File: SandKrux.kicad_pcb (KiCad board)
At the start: 2 copper layers, 58.3 x 98.2 mm, 177 parts, among them CN2 SM02B-PASS-TBT(LF)(SN), CN3 1.25mm-2P socket, IC1 TROPIC01_chip, Q1 S8050, SW1 TL3330AF130QG, SW2 TL3330AF130QG, SW3 TL3330AF130QG, SW4 TL3330AF130QG, SW5 TL3330AF130QG, U1 K210_C913414, U10 AXP173_C3345106, U12 PCIE-67P42H, U13 CH552T, U2 MT9700, U3 XC6206-3.3V, U4 XC6206P182MR_C347373, U5 GD25LQ128EWIGR, U6 TMI7003C, U7 SGM803-TXN3/TR_C5152602, U8 XC6206P302MR_C347375, U9 HX TF-CARD XG8P H1.5, X1 X322526MMB4SI

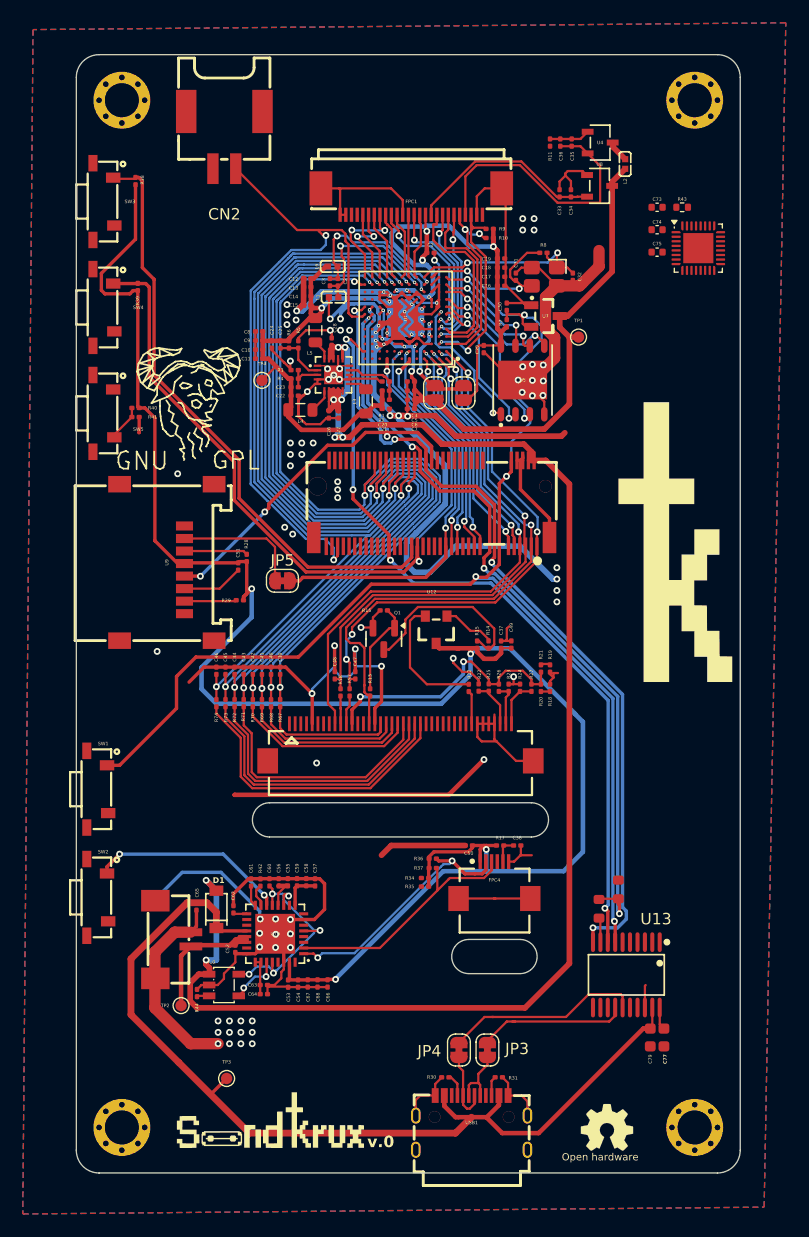
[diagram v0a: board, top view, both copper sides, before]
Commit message: troca de resistores por pecas jlcpcb
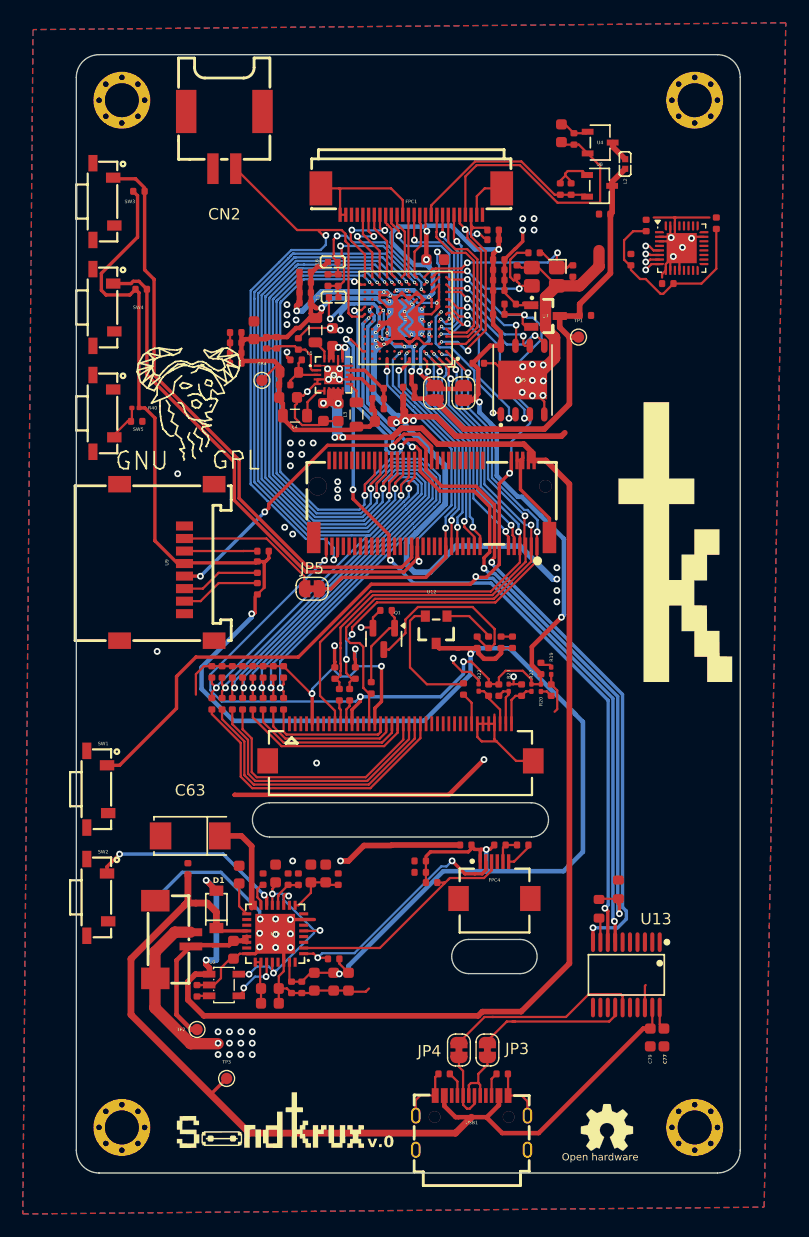
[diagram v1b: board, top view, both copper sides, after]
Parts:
- removed C61: 220uF, Capacitor_SMD:C_0201_0603Metric
- removed C64, C67, C68: 22uF, Capacitor_SMD:C_0201_0603Metric
- removed C65: 10uF, Capacitor_SMD:C_0201_0603Metric
- removed C73, C74, C75: 100n, Capacitor_SMD:C_0402_1005Metric
- removed R41: 0R, Resistor_SMD:R_0201_0603Metric
- removed R43: 47k, Resistor_SMD:R_0402_1005Metric
- removed R44: 10K, Resistor_SMD:R_0201_0603Metric
- removed R67, R68, R69, R70, R71, R72, R73, R74: 100R, Resistor_SMD:R_0201_0603Metric
- added C69: 1uF, PCM_JLCPCB:C_0603, F.Cu at (94.5, 160.7)
- added C70: 1uF, PCM_JLCPCB:C_0603, F.Cu at (97.7, 160.6)
- added C71: 100nF, PCM_JLCPCB:C_0402, F.Cu at (109.4, 118.8)
- added C72: 100nF, PCM_JLCPCB:C_0402, F.Cu at (109.4, 117.9)
- added C76: 10uF, PCM_JLCPCB:C_0402, F.Cu at (94.2, 115.8)
- added C78: 10uF, PCM_JLCPCB:C_0402, F.Cu at (94.2, 114.9)
- added C80: 10uF, PCM_JLCPCB:C_0402, F.Cu at (94.2, 114.0)
- added C81: 10uF, PCM_JLCPCB:C_0402, F.Cu at (94.2, 113.1)
- added R45: 150kΩ, PCM_JLCPCB:R_0402, F.Cu at (106.7, 118.9)
- added R46: 2kΩ, PCM_JLCPCB:R_0402, F.Cu at (116.8, 105.0)
- added R47: 100Ω, PCM_JLCPCB:R_0402, F.Cu at (116.4, 140.3)
- added R48: 5.1kΩ, PCM_JLCPCB:R_0402, F.Cu at (119.3, 144.5)
- added R54: 100Ω, PCM_JLCPCB:R_0402, F.Cu at (94.8, 145.7)
- added R55: 100Ω, PCM_JLCPCB:R_0402, F.Cu at (95.7, 145.7)
- added R56: 100Ω, PCM_JLCPCB:R_0402, F.Cu at (96.6, 145.7)
- added R59: 100Ω, PCM_JLCPCB:R_0402, F.Cu at (92.1, 145.7)
- added R60: 100Ω, PCM_JLCPCB:R_0402, F.Cu at (98.4, 145.7)
- added R61: 100Ω, PCM_JLCPCB:R_0402, F.Cu at (97.5, 145.7)
- C1, C52, C57: footprint Capacitor_SMD:C_0201_0603Metric -> PCM_JLCPCB:C_0603
- C10, C11: value 10uF -> 100nF; footprint Capacitor_SMD:C_0201_0603Metric -> PCM_JLCPCB:C_0402
- C12, C13, C14, C55, C58: value 10uF -> 22uF; footprint Capacitor_SMD:C_0201_0603Metric -> PCM_JLCPCB:C_0603
- C15, C16, C17: value 10uF -> 18pF; footprint Capacitor_SMD:C_0201_0603Metric -> PCM_JLCPCB:C_0402
- C18, C19, C49, C56: value 100nF -> 22uF; footprint Capacitor_SMD:C_0201_0603Metric -> PCM_JLCPCB:C_0603
- C2, C37, C39, C40, C50, C53, C8, C9: footprint Capacitor_SMD:C_0201_0603Metric -> PCM_JLCPCB:C_0402
- C20, C25: value 18pF -> 22uF; footprint Capacitor_SMD:C_0201_0603Metric -> PCM_JLCPCB:C_0603
- C21, C26, C27, C59, C66: value 22uF -> 10uF; footprint Capacitor_SMD:C_0201_0603Metric -> PCM_JLCPCB:C_0402
- C22, C24, C28: value 22uF -> 100nF; footprint Capacitor_SMD:C_0201_0603Metric -> PCM_JLCPCB:C_0402
- C23: value 18pF -> 6pF; footprint Capacitor_SMD:C_0201_0603Metric -> PCM_JLCPCB:C_0402
- C29, C30, C34, C38: value 100nF -> 100pF; footprint Capacitor_SMD:C_0201_0603Metric -> PCM_JLCPCB:C_0402
- C3: value 10uF -> 6pF; footprint Capacitor_SMD:C_0201_0603Metric -> PCM_JLCPCB:C_0402
- C31, C32: value 6pF -> 100pF; footprint Capacitor_SMD:C_0201_0603Metric -> PCM_JLCPCB:C_0402
- C33, C36: value 10uF -> 100pF; footprint Capacitor_SMD:C_0201_0603Metric -> PCM_JLCPCB:C_0402
- C35: value 22uF -> 100pF; footprint Capacitor_SMD:C_0201_0603Metric -> PCM_JLCPCB:C_0402
- C4, C5, C6, C7: value 100nF -> 10uF; footprint Capacitor_SMD:C_0201_0603Metric -> PCM_JLCPCB:C_0402
- C41, C43: value 100pF -> 10uF; footprint Capacitor_SMD:C_0201_0603Metric -> PCM_JLCPCB:C_0402
- C42, C44, C45, C46: value 100pF -> 100nF; footprint Capacitor_SMD:C_0201_0603Metric -> PCM_JLCPCB:C_0402
- C47, C48: value 100pF -> 22uF; footprint Capacitor_SMD:C_0201_0603Metric -> PCM_JLCPCB:C_0603
- C51: value 10uF -> 1nF; footprint Capacitor_SMD:C_0201_0603Metric -> PCM_JLCPCB:C_0402
- C54: value 1nF -> 100nF; footprint Capacitor_SMD:C_0201_0603Metric -> PCM_JLCPCB:C_0402
- C60, C62: value 1uF -> 100nF; footprint Capacitor_SMD:C_0201_0603Metric -> PCM_JLCPCB:C_0402
- C63: value 220nF -> TAJC227K006RNJ; footprint Capacitor_SMD:C_0201_0603Metric -> easyeda2kicad:CAP-SMD_L6.0-W3.2-R-RD
- R1: value 300k 1% -> 680kΩ; footprint Resistor_SMD:R_0201_0603Metric -> PCM_JLCPCB:R_0603
- R10: value 2K -> 100Ω; footprint Resistor_SMD:R_0201_0603Metric -> PCM_JLCPCB:R_0402
- R11: value 0R -> 100Ω; footprint Resistor_SMD:R_0201_0603Metric -> PCM_JLCPCB:R_0402
- R12: value 5.1R -> 100Ω; footprint Resistor_SMD:R_0201_0603Metric -> PCM_JLCPCB:R_0402
- R13: value 100R -> 10kΩ; footprint Resistor_SMD:R_0201_0603Metric -> PCM_JLCPCB:R_0402
- R14: value 100R -> 0Ω; footprint Resistor_SMD:R_0201_0603Metric -> PCM_JLCPCB:R_0402
- R15, R17, R28: value 10K -> 10kΩ; footprint Resistor_SMD:R_0201_0603Metric -> PCM_JLCPCB:R_0402
- R16: value 10K -> 0Ω; footprint Resistor_SMD:R_0201_0603Metric -> PCM_JLCPCB:R_0402
- R18, R21: value 0R -> 5.1kΩ; footprint Resistor_SMD:R_0201_0603Metric -> PCM_JLCPCB:R_0402
- R2, R3: value 150k 1% -> 150kΩ; footprint Resistor_SMD:R_0201_0603Metric -> PCM_JLCPCB:R_0402
- R24, R25, R26: value 5.1K -> 1.5kΩ; footprint Resistor_SMD:R_0201_0603Metric -> PCM_JLCPCB:R_0402
- R29: value 10K -> 47kΩ; footprint Resistor_SMD:R_0201_0603Metric -> PCM_JLCPCB:R_0402
- R30, R31: value 5.1K -> 5.1kΩ; footprint Resistor_SMD:R_0201_0603Metric -> PCM_JLCPCB:R_0402
- R34, R35, R36: value 1.5K -> 1.5kΩ; footprint Resistor_SMD:R_0201_0603Metric -> PCM_JLCPCB:R_0402
- R37, R38: value 1.5K -> 10kΩ; footprint Resistor_SMD:R_0201_0603Metric -> PCM_JLCPCB:R_0402
- R39: value 1.5K -> 200kΩ; footprint Resistor_SMD:R_0201_0603Metric -> PCM_JLCPCB:R_0402
- R4: value 680k 1% -> 12kΩ; footprint Resistor_SMD:R_0201_0603Metric -> PCM_JLCPCB:R_0402
- R42: value 200K -> 0Ω; footprint Resistor_SMD:R_0201_0603Metric -> PCM_JLCPCB:R_0402
- R5: value 150k 1% -> 300kΩ; footprint Resistor_SMD:R_0201_0603Metric -> PCM_JLCPCB:R_0402
- R57, R58: value 100R -> 100Ω; footprint Resistor_SMD:R_0201_0603Metric -> PCM_JLCPCB:R_0402
- R6: value 300k 1% -> 300kΩ; footprint Resistor_SMD:R_0201_0603Metric -> PCM_JLCPCB:R_0402
- R7: value 12K -> 1MΩ; footprint Resistor_SMD:R_0201_0603Metric -> PCM_JLCPCB:R_0402
- R8: value 1M -> 2kΩ; footprint Resistor_SMD:R_0201_0603Metric -> PCM_JLCPCB:R_0402
- R9: value 2K -> 5.1kΩ; footprint Resistor_SMD:R_0201_0603Metric -> PCM_JLCPCB:R_0402
- moved R38 71.3 mm to (90.8, 170.9), turned to -90 degrees
- moved C60 65.6 mm to (126.6, 102.7), turned to 180 degrees
- moved C62 60.6 mm to (124.9, 111.6), turned to 0 degrees
- moved C44 57.7 mm to (136.4, 103.5)
- moved C35 55.7 mm to (93.0, 142.9)
- moved C36 55.6 mm to (92.1, 142.9)
- moved C46 54.3 mm to (130.2, 103.7)
- moved R25 53.3 mm to (85.7, 100.7), turned to 0 degrees
- moved R39 53.2 mm to (96.6, 161.1), turned to -90 degrees
- moved C45 51.6 mm to (132.1, 108.8), turned to 180 degrees
- moved R11 51.6 mm to (104.2, 144.9), turned to 90 degrees
- moved C34 51.5 mm to (93.9, 142.9)
- moved C33 50.4 mm to (94.8, 142.9)
- moved R24 48.3 mm to (85.9, 109.3), turned to 0 degrees
- moved R29 45.5 mm to (128.9, 106.7), turned to 90 degrees
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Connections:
- C1 pad 1: /k210/1V8 -> /VCC_1V83V3
- C10 pad 1: GND -> /VCC_1V83V3
- C10 pad 2: /k210/0V9 -> GND
- C11 pad 1: GND -> /VCC_1V83V3
- C11 pad 2: /k210/0V9 -> GND
- C12 pad 1: GND -> /k210/0V9
- C12 pad 2: /k210/0V9 -> GND
- C13 pad 1: GND -> /k210/0V9
- C13 pad 2: /k210/0V9 -> GND
- C14 pad 1: GND -> /k210/0V9
- C14 pad 2: /k210/0V9 -> GND
- C15 pad 1: GND -> /k210/0V9
- C15 pad 2: /k210/0V9 -> /k210/Vadj
- C16 pad 1: GND -> /k210/0V9
- C16 pad 2: /k210/1V8 -> Net-(U6-FB2)
- C17 pad 1: GND -> /k210/0V9
- C17 pad 2: /k210/1V8 -> Net-(U6-FB3)
- C18 pad 1: GND -> /5V
- C18 pad 2: /k210/1V8 -> GND
- C19 pad 1: GND -> /5V
- C19 pad 2: /k210/1V8 -> GND
- C2 pad 1: Net-(U1-VSSPLL) -> GND
- C2 pad 2: Net-(U1-VDDPLL) -> /CH552_P1.0
- C20 pad 1: /k210/Vadj -> /5V
- C20 pad 2: /k210/0V9 -> GND
- C21 pad 1: GND -> Net-(U1-VDDPLL)
- C21 pad 2: /k210/0V9 -> Net-(U1-VSSPLL)
- C22 pad 1: GND -> Net-(U1-VDDPLL)
- C22 pad 2: /k210/0V9 -> Net-(U1-VSSPLL)
- C23 pad 1: Net-(U6-FB2) -> /k210/XIN
- C23 pad 2: /k210/0V9 -> GND
- C24 pad 1: GND -> /VCC_1V83V3
- C24 pad 2: /k210/0V9 -> GND
- C25 pad 1: Net-(U6-FB3) -> /k210/CMOS-AVDD
- C25 pad 2: /k210/0V9 -> GND
- C26 pad 1: GND -> /k210/CMOS-AVDD
- C26 pad 2: /5V -> GND
- C27 pad 1: GND -> /k210/CMOS-DVDD
- C27 pad 2: /5V -> GND
- C28 pad 1: GND -> /k210/CMOS-DVDD
- C28 pad 2: /5V -> GND
- C29 pad 1: /k210/1V8 -> GND
- C29 pad 2: GND -> /LCD_D0
- C3 pad 1: Net-(U1-VSSPLL) -> GND
- C3 pad 2: Net-(U1-VDDPLL) -> /k210/XOUT
- C30 pad 2: /CH552_P1.0 -> /LCD_D1
- C31 pad 1: /k210/XOUT -> GND
- C31 pad 2: GND -> /LCD_D2
- C32 pad 2: /k210/XIN -> /LCD_D3
- C33 pad 2: /k210/CMOS-DVDD -> /LCD_D4
- C34 pad 2: /k210/CMOS-DVDD -> /LCD_D5
- C35 pad 2: /k210/CMOS-AVDD -> /LCD_D6
- C36 pad 2: /k210/CMOS-AVDD -> /LCD_D7
- C38 pad 1: /CAPTOUCH_RST -> GND
- C38 pad 2: GND -> /CAPTOUCH_RST
- C39 pad 1: /LCD_D0 -> GND
- C39 pad 2: GND -> /LCD_WR
- C4 pad 1: GND -> /k210/0V9
- C4 pad 2: +3.3V -> GND
- C40 pad 1: /LCD_D1 -> GND
- C40 pad 2: GND -> /LCD_DC
- C41 pad 1: /LCD_D2 -> GND
- C41 pad 2: GND -> /3V3
- C42 pad 1: /LCD_D3 -> /3V3
- C43 pad 1: /LCD_D4 -> /3V3
- C44 pad 1: /LCD_D5 -> VCC
- C45 pad 1: /LCD_D6 -> VCC
- C46 pad 1: /LCD_D7 -> VCC
- C47 pad 1: /LCD_WR -> /3V3
- C48 pad 1: /LCD_DC -> /3V3
- C5 pad 1: GND -> /k210/0V9
- C5 pad 2: +3.3V -> GND
- C51 pad 1: GND -> /3V3
- C51 pad 2: /3V3 -> GND
- C52 pad 1: GND -> Net-(C52-Pad1)
- C52 pad 2: /VBAT -> GND
- C53 pad 1: GND -> /VDD
- C53 pad 2: /3V3 -> GND
- C54 pad 2: /3V3 -> /VDD
- C55 pad 1: /VDD -> /ADD_3V0
- C56 pad 1: /VDD -> /ADD_3V0
- C57 pad 1: GND -> /VBAT
- C57 pad 2: /ADD_3V0 -> GND
- C58 pad 1: GND -> Net-(C52-Pad1)
- C58 pad 2: /ADD_3V0 -> GND
- C59 pad 2: /ADD_3V0 -> /5V_USB
- C6 pad 1: GND -> /k210/0V9
- C6 pad 2: +3.3V -> GND
- C60 pad 1: /IPSOUT -> +3.3V
- C62 pad 1: Net-(U10-VINT) -> +3.3V
- C63 pad 1: Net-(C63-Pad1) -> Net-(U10-VREF)
- C66 pad 2: /3V3 -> /ADD_3V0
- C7 pad 1: GND -> /k210/0V9
- C7 pad 2: +3.3V -> GND
- C8 pad 1: GND -> /VCC_1V83V3
- C8 pad 2: /k210/0V9 -> GND
- C9 pad 1: GND -> /VCC_1V83V3
- C9 pad 2: /k210/0V9 -> GND
- FPC1 pad 11: /k210/1V8 -> /VCC_1V83V3
- JP1 pad 2: /k210/1V8 -> /VCC_1V83V3
- R1 pad 1: /k210/Vadj -> /k210/0V9
- R1 pad 2: GND -> Net-(U6-FB2)
- R10 pad 1: /k210/DVP_SCL -> Net-(FPC3-Pad10)
- R10 pad 2: /k210/1V8 -> /LCD_DC
- R11 pad 1: GND -> Net-(FPC3-Pad11)
- R11 pad 2: GND -> /LCD_WR
- R12 pad 1: Net-(FPC3-Pad33) -> /LCD_RST
- R12 pad 2: /LCD_BACKLIGHT -> Net-(Q1-B)
- R13 pad 1: /LCD_RST -> Net-(Q1-B)
- R13 pad 2: Net-(Q1-B) -> GND
- R14 pad 1: Net-(Q1-C) -> /VCC_6
- R14 pad 2: Net-(U3-VSS) -> GND
- R16 pad 1: GND -> /VCC_7
- R16 pad 2: Net-(Q1-B) -> /VCC_1V83V3
- R18 pad 1: /VCC_6 -> /IM0
- R18 pad 2: GND -> /VCC_1V83V3
- R2 pad 1: /k210/0V9 -> GND
- R2 pad 2: /k210/Vadj -> Net-(U6-FB2)
- R21 pad 1: /VCC_7 -> /IM1
- R24 pad 1: /IM2 -> /3V3
- R24 pad 2: GND -> /KEY1
- R25 pad 1: /IM0 -> /3V3
- R25 pad 2: /VCC_1V83V3 -> /KEY2
- R26 pad 1: /IM1 -> /3V3
- R26 pad 2: /VCC_1V83V3 -> /I2C_SCL
- R28 pad 1: /SPI1_MOSI -> /3V3
- R28 pad 2: /3V3 -> Net-(U9-DAT0)
- R29 pad 1: Net-(U9-DAT0) -> /SPI_MISO
- R29 pad 2: /3V3 -> VCC
- R3 pad 1: Net-(U6-FB2) -> GND
- R3 pad 2: GND -> Net-(U6-FB3)
- R34 pad 1: /IO17 -> /3V3
- R34 pad 2: /3V3 -> /I2C_SDA
- R35 pad 1: /IO19 -> /IO17
- R36 pad 1: /3V3 -> /IO19
- R36 pad 2: /I2C_SDA -> /3V3
- R37 pad 2: /I2C_SCL -> /SPI1_MOSI
- R38 pad 1: /3V3 -> GND
- R38 pad 2: /KEY2 -> /ISET
- R39 pad 1: /3V3 -> GND
- R39 pad 2: /KEY1 -> Net-(U10-BIAS)
- R4 pad 1: /k210/0V9 -> /VCC_1V83V3
- R4 pad 2: Net-(U6-FB2) -> /CH552_P1.0
- R42 pad 1: GND -> Net-(R40-Pad1)
- R42 pad 2: Net-(U10-BIAS) -> GND
- R5 pad 1: Net-(U6-FB3) -> /k210/0V9
- R5 pad 2: GND -> Net-(U6-FB3)
- R57 pad 1: Net-(FPC3-Pad11) -> Net-(FPC3-Pad22)
- R57 pad 2: /LCD_WR -> /LCD_D5
- R58 pad 1: Net-(FPC3-Pad10) -> Net-(FPC3-Pad23)
- R58 pad 2: /LCD_DC -> /LCD_D6
- R6 pad 1: /k210/0V9 -> GND
- R6 pad 2: Net-(U6-FB3) -> /k210/Vadj
- R7 pad 1: /k210/1V8 -> /k210/XOUT
- R7 pad 2: /CH552_P1.0 -> /k210/XIN
- R8 pad 1: /k210/XOUT -> /k210/DVP_SDA
- R8 pad 2: /k210/XIN -> /VCC_1V83V3
- R9 pad 1: /k210/DVP_SDA -> Net-(FPC3-Pad33)
- R9 pad 2: /k210/1V8 -> /LCD_BACKLIGHT
- U1 pad H3: /k210/1V8 -> /VCC_1V83V3
- U1 pad J3: /k210/1V8 -> /VCC_1V83V3
- U1 pad K6: /k210/1V8 -> /VCC_1V83V3
- U1 pad K8: /k210/1V8 -> /VCC_1V83V3
- U10 pad 25: Net-(C63-Pad1) -> Net-(C52-Pad1)
- U10 pad 26: Net-(C63-Pad1) -> Net-(C52-Pad1)
- U12 pad 75: unconnected-(U12-Pad75) -> /VCC_1V83V3
- U5 pad 8: /k210/1V8 -> /VCC_1V83V3
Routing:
- net /VCC_1V83V3: track 24.1 -> 131.4 mm, vias 2 -> 11
- net /k210/1V8: track 47.6 -> 0.00 mm, vias 6 -> 0
- net (no net): track 0.00 -> 27.9 mm, vias 0 -> 8
- net GND: track 506.7 -> 484.1 mm, vias 89 -> 91
- net VCC: track 0.00 -> 17.9 mm
- net Net-(U10-VREF): track 1.84 -> 8.97 mm
- net /k210/0V9: track 93.1 -> 97.6 mm
- net /3V3: track 166.3 -> 170.7 mm
- net Net-(C52-Pad1): track 0.00 -> 4.17 mm
- net +3.3V: track 58.8 -> 55.0 mm
- net Net-(C63-Pad1): track 3.33 -> 0.00 mm
- net /5V_USB: track 83.8 -> 86.6 mm
- net Net-(U9-DAT0): track 4.57 -> 7.06 mm
- net /SPI1_CS_TF: track 35.6 -> 33.3 mm
- net /5V: track 141.0 -> 143.3 mm
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
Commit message: TROPCAL 01 CONECTIO E ATUALIZACAO E SUBSTITUICAO DE COMPONENTES POR COMPONENTES JLC DISPONIVEIS
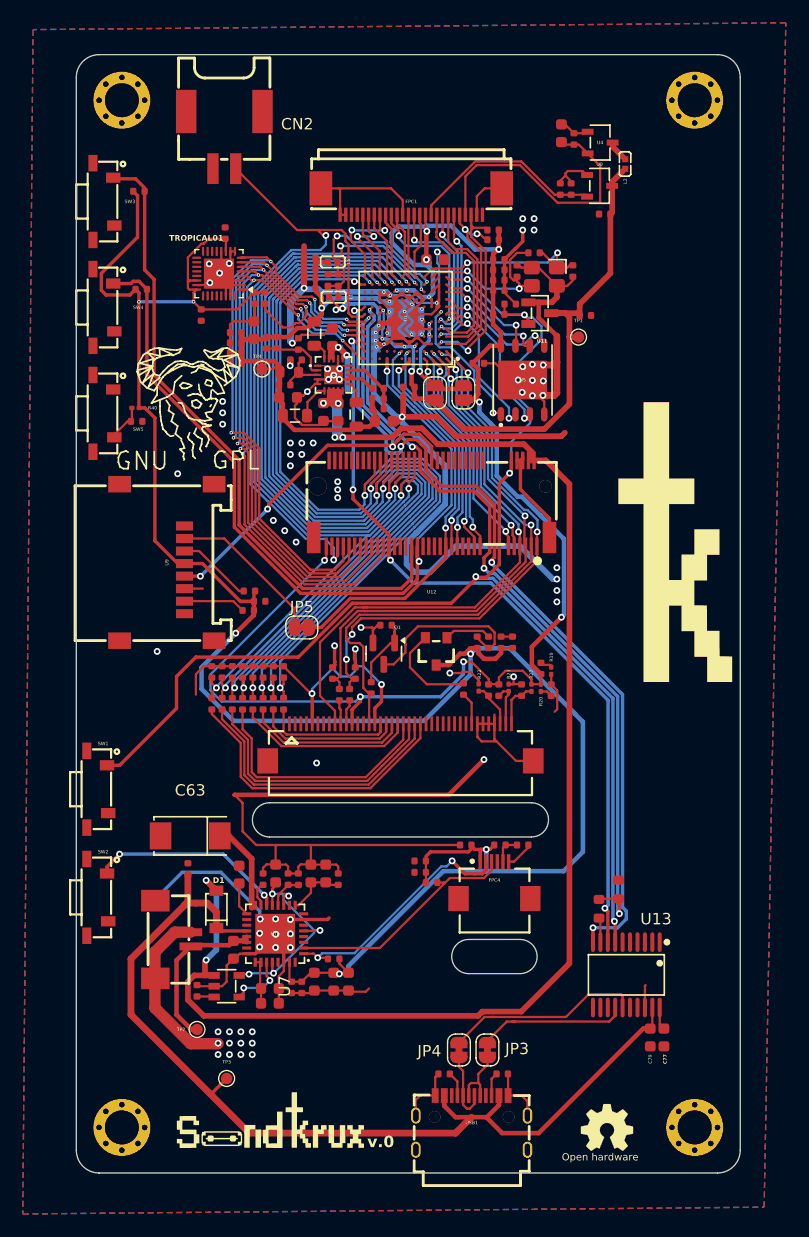
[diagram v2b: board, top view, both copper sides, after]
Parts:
- removed L5: 2.2uH, Inductor_SMD:L_0805_2012Metric
- removed U2: MT9700, easyeda2kicad:SOT-23-5_L3.0-W1.7-P0.95-LS2.8-BR
- added L8: 2.2uH,50mA, PCM_JLCPCB:L_0805, F.Cu at (104.8, 120.3)
- added U11: APX803-31SAG-7, easyeda2kicad:SOT-23-3_L2.9-W1.3-P1.90-LS2.4-BR, F.Cu at (120.9, 111.4)
- IC1: value TROPIC01_chip -> TR01-P2; footprint easyeda2kicad:QFN-32-1EP_4x4mm_P0.4mm_EP2.65x2.65mm -> Package_DFN_QFN:QFN-32-1EP_4x4mm_P0.4mm_EP2.65x2.65mm
- L3, L4: value 2.2uH -> 2.2uH,50mA; footprint Inductor_SMD:L_0805_2012Metric -> PCM_JLCPCB:L_0805
- U7: value SGM803-TXN3/TR_C5152602 -> MT9700-N; footprint easyeda2kicad:SOT-23-3_L2.9-W1.5-P1.90-LS2.6-BR -> easyeda2kicad:SOT-23-5_L2.9-W1.6-P0.95-LS2.9-BL
- moved U7 65.2 mm to (93.4, 170.5), turned to -90 degrees
- moved C44 45.9 mm to (91.2, 111.6), turned to -90 degrees
- moved IC1 40.7 mm to (92.7, 107.9), turned to 180 degrees
- moved C45 39.1 mm to (93.3, 104.4), turned to 90 degrees
- moved C46 35.0 mm to (95.9, 110.1), turned to -90 degrees
- moved R29 32.3 mm to (96.8, 110.1)
- moved L4 7.40 mm to (101.1, 113.2), turned to -90 degrees
- moved L3 5.40 mm to (99.4, 120.4), turned to 0 degrees
- moved R37 3.70 mm to (95.4, 135.8)
- moved JP5 3.52 mm to (100.0, 139.0)
- moved C43 3.01 mm to (96.3, 136.7), turned to 0 degrees
- moved R28 2.06 mm to (95.3, 137.5), turned to 180 degrees
- moved U3 1.90 mm to (111.8, 141.1)
- moved C4 1.36 mm to (100.7, 109.2)
- moved C5 1.31 mm to (100.7, 108.3)
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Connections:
- C44 pad 1: VCC -> /3V3
- C45 pad 1: VCC -> /3V3
- C46 pad 1: VCC -> /3V3
- IC1 pad 1: (no net) -> /3V3
- IC1 pad 10: (no net) -> GND
- IC1 pad 11: (no net) -> /3V3
- IC1 pad 12: (no net) -> GND
- IC1 pad 13: (no net) -> unconnected-(IC1-DNC-Pad13)
- IC1 pad 14: (no net) -> unconnected-(IC1-DNC-Pad14)
- IC1 pad 15: (no net) -> unconnected-(IC1-NC-Pad15)
- IC1 pad 16: (no net) -> unconnected-(IC1-NC-Pad16)
- IC1 pad 17: (no net) -> unconnected-(IC1-DNC-Pad17)
- IC1 pad 18: (no net) -> unconnected-(IC1-DNC-Pad18)
- IC1 pad 19: (no net) -> unconnected-(IC1-DNC-Pad19)
- IC1 pad 2: (no net) -> GND
- IC1 pad 20: (no net) -> unconnected-(IC1-DNC-Pad20)
- IC1 pad 21: (no net) -> unconnected-(IC1-DNC-Pad21)
- IC1 pad 22: (no net) -> /3V3
- IC1 pad 23: (no net) -> GND
- IC1 pad 24: (no net) -> /3V3
- IC1 pad 25: (no net) -> unconnected-(IC1-NC-Pad25)
- IC1 pad 26: (no net) -> unconnected-(IC1-DNC-Pad26)
- IC1 pad 27: (no net) -> unconnected-(IC1-DNC-Pad27)
- IC1 pad 28: (no net) -> unconnected-(IC1-DNC-Pad28)
- IC1 pad 29: (no net) -> unconnected-(IC1-DNC-Pad29)
- IC1 pad 3: (no net) -> GND
- IC1 pad 30: (no net) -> GND
- IC1 pad 31: (no net) -> GND
- IC1 pad 32: (no net) -> unconnected-(IC1-NC-Pad32)
- IC1 pad 33: (no net) -> GND
- IC1 pad 4: (no net) -> /TP_GPO
- IC1 pad 5: (no net) -> /TP_SPI_MOSI
- IC1 pad 6: (no net) -> /TP_SPI_MISO
- IC1 pad 7: (no net) -> /TP_SPI_SCK
- IC1 pad 8: (no net) -> /TP_SPI_CS
- IC1 pad 9: (no net) -> GND
- L3 pad 2: Net-(U6-SW1) -> Net-(U6-SW2)
- L4 pad 2: Net-(U6-SW2) -> Net-(U6-SW3)
- R29 pad 1: /SPI_MISO -> /TP_SPI_MISO
- R29 pad 2: VCC -> /3V3
- U1 pad A12: /k210/IO_17 -> /TP_GPO
- U1 pad C10: GND -> unconnected-(U1-VSS-PadC10)
- U1 pad C12: /k210/IO_15 -> /TP_SPI_MOSI
- U1 pad C4: GND -> unconnected-(U1-VSS-PadC4)
- U1 pad C6: GND -> unconnected-(U1-VSS-PadC6)
- U1 pad C9: GND -> unconnected-(U1-VSS-PadC9)
- U1 pad D12: /k210/IO_13 -> /TP_SPI_MISO
- U1 pad D5: GND -> unconnected-(U1-VSS-PadD5)
- U1 pad D6: /k210/0V9 -> unconnected-(U1-VDD-PadD6)
- U1 pad D7: GND -> unconnected-(U1-VSS-PadD7)
- U1 pad D8: GND -> unconnected-(U1-VSS-PadD8)
- U1 pad D9: /k210/0V9 -> unconnected-(U1-VDD-PadD9)
- U1 pad E10: GND -> unconnected-(U1-VSS-PadE10)
- U1 pad E12: /k210/IO_11 -> /TP_SPI_SCK
- U1 pad E3: GND -> unconnected-(U1-VSS-PadE3)
- U1 pad E4: GND -> unconnected-(U1-VSS-PadE4)
- U1 pad E5: GND -> unconnected-(U1-VSS-PadE5)
- U1 pad E6: GND -> unconnected-(U1-VSS-PadE6)
- U1 pad E7: /k210/0V9 -> unconnected-(U1-VDD-PadE7)
- U1 pad E8: GND -> unconnected-(U1-VSS-PadE8)
- U1 pad E9: /k210/0V9 -> unconnected-(U1-VDD-PadE9)
- U1 pad F10: GND -> unconnected-(U1-VSS-PadF10)
- U1 pad F12: /k210/IO_9 -> /TP_SPI_CS
- U1 pad F4: /k210/0V9 -> unconnected-(U1-VDD-PadF4)
- U1 pad F5: GND -> unconnected-(U1-VSS-PadF5)
- U1 pad F6: /k210/0V9 -> unconnected-(U1-VDD-PadF6)
- U1 pad F7: GND -> unconnected-(U1-VSS-PadF7)
- U1 pad F8: GND -> unconnected-(U1-VSS-PadF8)
- U1 pad F9: GND -> unconnected-(U1-VSS-PadF9)
- U1 pad G3: GND -> unconnected-(U1-VSS-PadG3)
- U1 pad G4: GND -> unconnected-(U1-VSS-PadG4)
- U1 pad G5: GND -> unconnected-(U1-VSS-PadG5)
- U1 pad G6: GND -> unconnected-(U1-VSS-PadG6)
- U1 pad G7: /k210/0V9 -> unconnected-(U1-VDD-PadG7)
- U1 pad G8: GND -> unconnected-(U1-VSS-PadG8)
- U1 pad G9: /k210/0V9 -> unconnected-(U1-VDD-PadG9)
- U1 pad H2: GND -> unconnected-(U1-VSS-PadH2)
- U1 pad H4: /k210/0V9 -> unconnected-(U1-VDD-PadH4)
- U1 pad H5: GND -> unconnected-(U1-VSS-PadH5)
- U1 pad H6: /k210/0V9 -> unconnected-(U1-VDD-PadH6)
- U1 pad H7: GND -> unconnected-(U1-VSS-PadH7)
- U1 pad H8: GND -> unconnected-(U1-VSS-PadH8)
- U1 pad H9: GND -> unconnected-(U1-VSS-PadH9)
- U1 pad J10: GND -> unconnected-(U1-VSS-PadJ10)
- U1 pad J2: GND -> unconnected-(U1-VSS-PadJ2)
- U1 pad J4: GND -> unconnected-(U1-VSS-PadJ4)
- U1 pad J5: /k210/0V9 -> unconnected-(U1-VDD-PadJ5)
- U1 pad J6: GND -> unconnected-(U1-VSS-PadJ6)
- U1 pad J7: /k210/0V9 -> unconnected-(U1-VDD-PadJ7)
- U1 pad J8: GND -> unconnected-(U1-VSS-PadJ8)
- U1 pad K10: GND -> unconnected-(U1-VSS-PadK10)
- U1 pad K2: GND -> unconnected-(U1-VSS-PadK2)
- U1 pad K3: GND -> unconnected-(U1-VSS-PadK3)
- U1 pad K5: GND -> unconnected-(U1-VSS-PadK5)
- U1 pad K7: GND -> unconnected-(U1-VSS-PadK7)
- U1 pad K9: GND -> unconnected-(U1-VSS-PadK9)
- U12 pad 55: unconnected-(U12-Pad55) -> /TP_GPO
- U12 pad 59: unconnected-(U12-Pad59) -> /TP_SPI_MOSI
- U12 pad 63: unconnected-(U12-Pad63) -> /TP_SPI_MISO
- U12 pad 67: unconnected-(U12-Pad67) -> /TP_SPI_SCK
- U12 pad 69: unconnected-(U12-Pad69) -> /TP_SPI_CS
- U7 pad 1: GND -> /5V
- U7 pad 2: /CH552_P1.0 -> GND
- U7 pad 3: +3.3V -> /ISET
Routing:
- net /TP_SPI_MISO: track 0.00 -> 57.5 mm, vias 0 -> 4
- net /TP_GPO: track 0.00 -> 52.2 mm, vias 0 -> 4
- net /TP_SPI_CS: track 0.00 -> 51.8 mm, vias 0 -> 4
- net /TP_SPI_MOSI: track 0.00 -> 51.8 mm, vias 0 -> 4
- net /TP_SPI_SCK: track 0.00 -> 51.6 mm, vias 0 -> 4
- net GND: track 484.1 -> 524.5 mm, vias 91 -> 89
- net (no net): track 27.9 -> 0.00 mm, vias 8 -> 0
- net /3V3: track 170.7 -> 190.7 mm, vias 4 -> 6
- net VCC: track 17.9 -> 0.00 mm
- net /KEY2: track 52.8 -> 56.8 mm
- net /KEY1: track 68.1 -> 72.1 mm
- net /LCD_BACKLIGHT: track 11.0 -> 8.52 mm
- net /SPI1_CS_TF: track 33.3 -> 35.6 mm
- net +3.3V: track 55.0 -> 57.1 mm
- net Net-(U9-DAT0): track 7.06 -> 5.44 mm
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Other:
- board text added: "TROPICAL01"
